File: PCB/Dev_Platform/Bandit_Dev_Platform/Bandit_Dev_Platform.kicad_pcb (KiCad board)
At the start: 4 copper layers, 50 x 30 mm, 108 parts, among them J1 Conn_01x03_Pin, J10 Conn_01x05_Pin, J11 Conn_01x05_Pin, J3 Conn_01x05_Pin, J4 Conn_01x05_Pin, J8 Conn_01x05_Pin, J9 Conn_01x06_Pin, P1 USB_C_Plug_USB2.0, SW1 SW_SPST, U1 AD7253, U2 RP2040, U3 AP2210N-4.0TRG1, U4 NCP164ASNADJT1G, U5 W25Q32JVSS, U6 MCP6486UT-E/OT, U7 MCP6S92-E/SN, U8 OPA1664, U9 OPA1664, Y1 12MHz

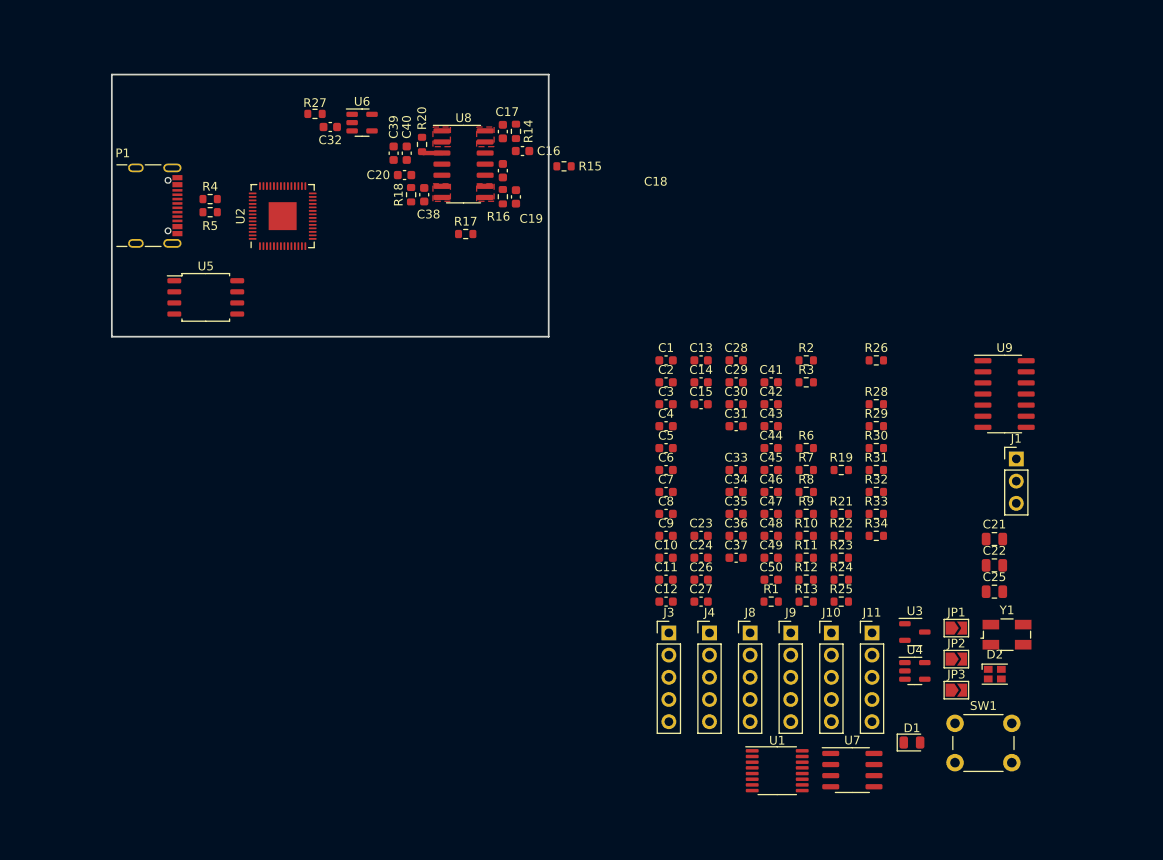
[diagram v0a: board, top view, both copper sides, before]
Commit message: update pcb, filter kinda done
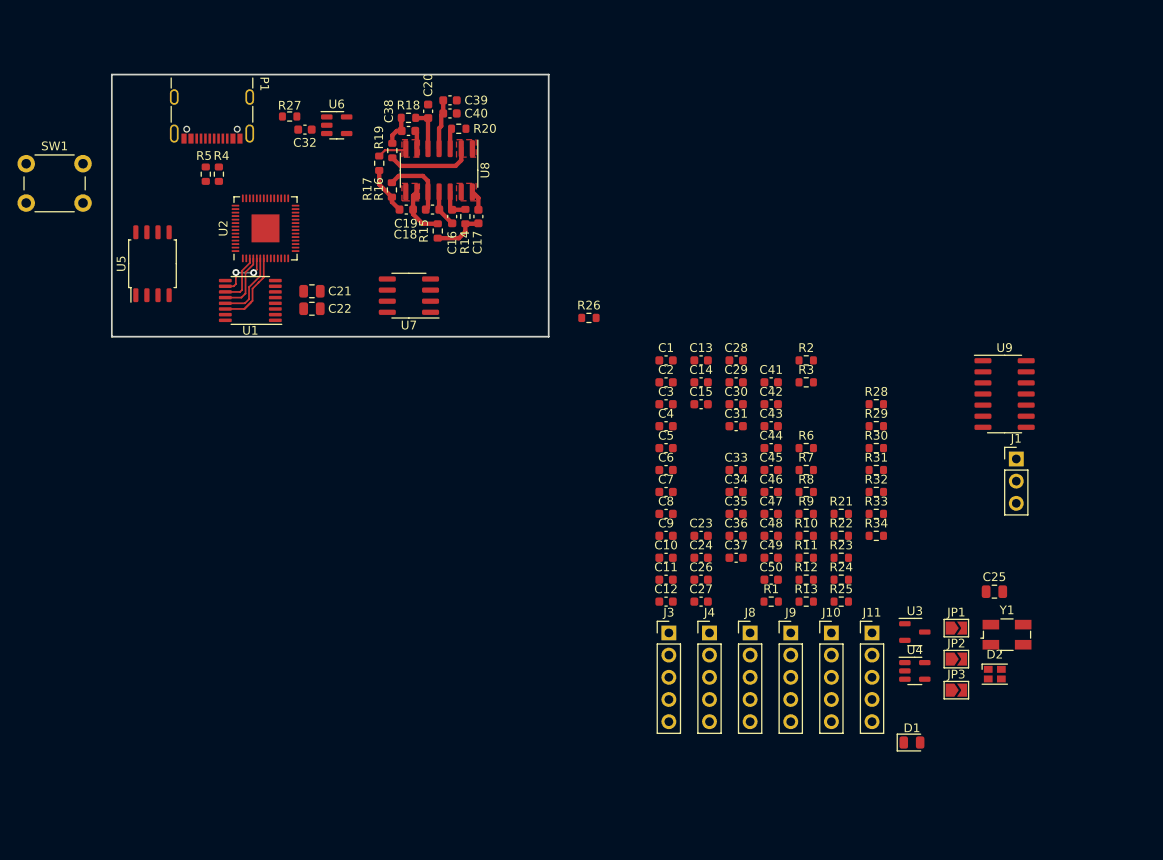
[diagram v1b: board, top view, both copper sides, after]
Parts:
- C16: value 15p C0G -> 15p C0G
- C17: value 330p C0G -> 330p C0G
- C19: value 150p C0G -> 150p C0G
- C38: value 100p C0G -> 100p C0G
- moved SW1 124.1 mm to (10.2, 30.2)
- moved C22 83.4 mm to (42.9, 46.8)
- moved C21 83.1 mm to (42.9, 44.8)
- moved U1 80.8 mm to (35.9, 45.9), turned to 180 degrees
- moved U7 74.3 mm to (54.0, 45.3), turned to 180 degrees
- moved R19 63.1 mm to (52.1, 28.7), turned to 90 degrees
- moved R26 33.2 mm to (74.6, 47.9)
- moved R15 16.2 mm to (57.3, 37.9), turned to -90 degrees
- moved P1 13.7 mm to (31.5, 23.6), turned to 180 degrees
- moved R17 12.8 mm to (50.6, 30.1), turned to -90 degrees
- moved R16 12.7 mm to (52.0, 33.2)
- moved C19 12.6 mm to (53.7, 35.5), turned to 180 degrees
- moved R14 11.3 mm to (60.5, 36.2), turned to 90 degrees
- moved C16 11.0 mm to (59.0, 36.2), turned to 90 degrees
- moved C17 10.1 mm to (62.0, 36.2), turned to -90 degrees
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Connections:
- C25 pad 2: Net-(U7-CH1) -> Net-(U7-CH0)
- R25 pad 2: Net-(U7-CH1) -> Net-(U7-CH0)
- R26 pad 1: Net-(U7-CH1) -> Net-(U7-CH0)
- U7 pad 2: /WGN_OUT -> Net-(U7-CH0)
- U7 pad 3: Net-(U7-CH1) -> /WGN_OUT
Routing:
- net Net-(U8A--): track 0.00 -> 10.7 mm
- net /ADC_SDO_B: track 0.00 -> 9.92 mm
- net /ADC_SDO_A: track 0.00 -> 8.11 mm
- net Net-(U8C-+): track 0.00 -> 8.07 mm
- net /ADC_SCK: track 0.00 -> 6.89 mm
- net /ADC_SDI: track 0.00 -> 6.47 mm, vias 0 -> 2
- net Net-(U8C--): track 0.00 -> 6.01 mm
- net /ADC_CSN: track 0.00 -> 5.99 mm
- net Net-(C17-Pad2): track 0.00 -> 5.89 mm
- net VDDA: track 0.00 -> 5.72 mm
- net Net-(U8B--): track 0.00 -> 5.49 mm
- net Net-(C19-Pad2): track 0.00 -> 5.44 mm
- net Net-(U8B-+): track 0.00 -> 4.94 mm
- net GNDA: track 0.00 -> 4.22 mm
- net Net-(C38-Pad2): track 0.00 -> 3.73 mm
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
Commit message: Josh said the tracks are great
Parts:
- removed C10, C7: 15p COG, Capacitor_SMD:C_0603_1608Metric
- removed Y1: 12MHz, Crystal:Crystal_SMD_EuroQuartz_MJ-4Pin_5.0x3.2mm
- added C17: 100n, Capacitor_SMD:C_0603_1608Metric, F.Cu at (52.4, 70.2)
- added C18: 10n, Capacitor_SMD:C_0603_1608Metric, F.Cu at (52.4, 72.7)
- added C51: 15p C0G, Capacitor_SMD:C_0603_1608Metric, F.Cu at (52.5, 45.1)
- added C52: 330p C0G, Capacitor_SMD:C_0603_1608Metric, F.Cu at (52.5, 48.1)
- added C53: 47p C0G, Capacitor_SMD:C_0603_1608Metric, F.Cu at (53.4, 42.9)
- added C54: 150p C0G, Capacitor_SMD:C_0603_1608Metric, F.Cu at (53.4, 39.9)
- added C55: 68p C0G, Capacitor_SMD:C_0603_1608Metric, F.Cu at (64.6, 42.4)
- added C56: 100p C0G, Capacitor_SMD:C_0603_1608Metric, F.Cu at (62.4, 40.1)
- added C57: 100n, Capacitor_SMD:C_0603_1608Metric, F.Cu at (65.8, 44.9)
- added C58: 10n, Capacitor_SMD:C_0603_1608Metric, F.Cu at (64.3, 44.9)
- added J5: BNC, ADS8584SIPM:BNC_THT, F.Cu at (75.9, 44.4)
- added J6: BNC, ADS8584SIPM:BNC_THT, F.Cu at (75.9, 27.6)
- added R35: 15k1, Resistor_SMD:R_0603_1608Metric, F.Cu at (52.5, 46.6)
- added R36: 8k4, Resistor_SMD:R_0603_1608Metric, F.Cu at (50.9, 43.5)
- added R37: 15k2, Resistor_SMD:R_0603_1608Metric, F.Cu at (55.6, 38.2)
- added R38: 5k9, Resistor_SMD:R_0603_1608Metric, F.Cu at (58.6, 36.8)
- added R39: 14k8, Resistor_SMD:R_0603_1608Metric, F.Cu at (63.9, 40.1)
- added R40: 6k3, Resistor_SMD:R_0603_1608Metric, F.Cu at (60.1, 38.3)
- added R41: 11k7, Resistor_SMD:R_0603_1608Metric, F.Cu at (62.6, 45.9)
- added U10: OPA1664, Package_SO:SOIC-14_3.9x8.7mm_P1.27mm, F.Cu at (57.9, 43.6)
- added X1: SG-210STF, Oscillator:Oscillator_SMD_SeikoEpson_SG210-4Pin_2.5x2.0mm, F.Cu at (41.1, 28.9)
- moved C25 71.6 mm to (68.5, 30.5), turned to 90 degrees
- moved R22 67.7 mm to (44.2, 40.0), turned to 180 degrees
- moved R24 66.8 mm to (44.2, 47.1), turned to 180 degrees
- moved R21 65.9 mm to (44.2, 41.5), turned to 180 degrees
- moved R23 65.0 mm to (44.2, 48.6), turned to 180 degrees
- moved R25 64.5 mm to (66.5, 27.5), turned to -90 degrees
- moved C23 55.7 mm to (41.9, 40.8), turned to -90 degrees
- moved C24 53.2 mm to (41.9, 47.9), turned to 90 degrees
- moved R26 22.5 mm to (65.0, 27.5), turned to 90 degrees
- moved U7 16.0 mm to (64.3, 33.0), turned to -90 degrees
- moved C52 15.0 mm to (47.0, 35.5), turned to 180 degrees
- moved P1 14.5 mm to (23.7, 35.9), turned to -90 degrees
- moved R36 13.9 mm to (45.3, 30.9), turned to 180 degrees
- moved R35 13.7 mm to (47.0, 34.0), turned to 0 degrees
- moved C51 12.6 mm to (47.0, 32.5), turned to 0 degrees
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- renumbered C16 to C51, C17 to C52, C18 to C53, C19 to C54, C20 to C55, C38 to C56, C39 to C57, C40 to C58, R14 to R35, R15 to R36, R16 to R37, R17 to R38, R18 to R39, R19 to R40, R20 to R41, U8 to U10
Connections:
- R22 pad 1: /SE_SIG_B -> /SE_SIG_A
- R23 pad 1: /SE_SIG_A -> /SE_SIG_B
- U2 pad 20: /XIN -> /CLK_12M
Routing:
- net /WGN_OUT: track 0.00 -> 60.2 mm
- net /SIG_IN: track 0.00 -> 21.4 mm
- net Net-(J2-In): track 0.00 -> 16.0 mm
- net /SE_SIG_B: track 0.00 -> 11.2 mm
- net Net-(U10A--): track 10.7 -> 21.3 mm
- net Net-(U10C-+): track 8.07 -> 16.1 mm
- net Net-(U7-CH0): track 0.00 -> 6.31 mm
- net Net-(U10C--): track 6.01 -> 12.0 mm
- net /SE_SIG_A: track 2.34 -> 8.23 mm
- net Net-(C52-Pad2): track 5.89 -> 11.8 mm
- net VDDA: track 5.72 -> 11.4 mm
- net Net-(U1-AINP_B): track 0.00 -> 5.54 mm
- net Net-(U1-AINP_A): track 0.00 -> 5.50 mm
- net Net-(U10B--): track 5.49 -> 11.0 mm
- net Net-(C54-Pad2): track 5.44 -> 10.9 mm
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- added copper zone on F.Cu, net /SE_SIG_B
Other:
- board size 50 x 30 mm -> 63.5 x 31.8 mm

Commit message: Fixing dev pcb
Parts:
- removed the C51 at (52.5, 45.1)
- removed the C51 at (47.0, 32.5)
- removed the C52 at (47.0, 35.5)
- removed the C52 at (52.5, 48.1)
- removed the C53 at (47.8, 30.2)
- removed the C53 at (53.4, 42.9)
- removed the C54 at (47.8, 27.2)
- removed the C54 at (53.4, 39.9)
- removed the C55 at (59.0, 29.8)
- removed the C55 at (64.6, 42.4)
- removed the C56 at (62.4, 40.1)
- removed the C56 at (56.8, 27.5)
- removed the C57 at (60.2, 32.2)
- removed the C57 at (65.8, 44.9)
- removed the C58 at (58.8, 32.2)
- removed the C58 at (64.3, 44.9)
- removed the R35 at (47.0, 34.0)
- removed the R35 at (52.5, 46.6)
- removed the R36 at (45.3, 30.9)
- removed the R36 at (50.9, 43.5)
- removed the R37 at (50.0, 25.6)
- removed the R37 at (55.6, 38.2)
- removed the R38 at (53.0, 24.1)
- removed the R38 at (58.6, 36.8)
- removed the R39 at (58.2, 27.5)
- removed the R39 at (63.9, 40.1)
- removed the R40 at (54.5, 25.6)
- removed the R40 at (60.1, 38.3)
- removed the R41 at (62.6, 45.9)
- removed the R41 at (57.0, 33.2)
- removed the U10 at (57.9, 43.6)
- removed the U10 at (52.2, 31.0)
- added C10: 15p COG, Capacitor_SMD:C_0603_1608Metric, F.Cu at (91.5, 80.9)
- added C51: 15p C0G, Capacitor_SMD:C_0603_1608Metric, F.Cu at (103.5, 70.9)
- added C52: 330p C0G, Capacitor_SMD:C_0603_1608Metric, F.Cu at (103.5, 73.4)
- added C53: 47p C0G, Capacitor_SMD:C_0603_1608Metric, F.Cu at (103.5, 75.9)
- added C54: 150p C0G, Capacitor_SMD:C_0603_1608Metric, F.Cu at (103.5, 78.4)
- added C55: 68p C0G, Capacitor_SMD:C_0603_1608Metric, F.Cu at (103.5, 80.9)
- added C56: 100p C0G, Capacitor_SMD:C_0603_1608Metric, F.Cu at (103.5, 83.5)
- added C57: 100n, Capacitor_SMD:C_0603_1608Metric, F.Cu at (103.5, 86.0)
- added C58: 10n, Capacitor_SMD:C_0603_1608Metric, F.Cu at (107.5, 58.4)
- added C7: 15p COG, Capacitor_SMD:C_0603_1608Metric, F.Cu at (91.5, 73.4)
- added R35: 15k1, Resistor_SMD:R_0603_1608Metric, F.Cu at (115.5, 68.4)
- added R36: 8k4, Resistor_SMD:R_0603_1608Metric, F.Cu at (115.5, 70.9)
- added R37: 15k2, Resistor_SMD:R_0603_1608Metric, F.Cu at (115.5, 73.4)
- added R38: 5k9, Resistor_SMD:R_0603_1608Metric, F.Cu at (115.5, 75.9)
- added R39: 14k8, Resistor_SMD:R_0603_1608Metric, F.Cu at (115.5, 78.4)
- added R40: 6k3, Resistor_SMD:R_0603_1608Metric, F.Cu at (115.5, 80.9)
- added R41: 11k7, Resistor_SMD:R_0603_1608Metric, F.Cu at (115.5, 83.5)
- added U10: OPA1664, Package_SO:SOIC-14_3.9x8.7mm_P1.27mm, F.Cu at (63.3, 32.0)
- added Y1: 12MHz, Crystal:Crystal_SMD_EuroQuartz_MJ-4Pin_5.0x3.2mm, F.Cu at (110.3, 104.5)
- moved SW1 133.8 mm to (129.1, 91.7)
- moved U6 113.1 mm to (120.1, 100.8), turned to 0 degrees
- moved X1 110.9 mm to (136.7, 85.3), turned to 0 degrees
- moved C22 94.1 mm to (135.6, 61.6)
- moved C21 94.0 mm to (135.6, 58.6)
- moved R27 91.0 mm to (111.5, 78.4), turned to 0 degrees
- moved U7 81.6 mm to (102.4, 105.2), turned to 0 degrees
- moved C25 75.3 mm to (135.6, 64.6), turned to 0 degrees
- moved C32 73.0 mm to (99.5, 60.9), turned to 0 degrees
- moved R22 72.1 mm to (111.5, 65.9), turned to 0 degrees
- moved R24 71.4 mm to (111.5, 70.9), turned to 0 degrees
- moved R21 70.8 mm to (111.5, 63.4), turned to 0 degrees
- moved R23 70.2 mm to (111.5, 68.4), turned to 0 degrees
- moved R26 67.1 mm to (111.5, 75.9), turned to 0 degrees
- moved J6 66.1 mm to (123.1, 73.9)
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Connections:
- C44 pad 2: Net-(U9C-+) -> Net-(U9A-+)
- C45 pad 1: Net-(U9C--) -> Net-(U9A--)
- C50 pad 2: Net-(U9A-+) -> Net-(U9C-+)
- R29 pad 1: Net-(U9C--) -> Net-(U9A--)
- R30 pad 2: Net-(U9C-+) -> Net-(U9A-+)
- R33 pad 1: Net-(U9A--) -> Net-(U9C--)
- R34 pad 2: Net-(U9A-+) -> Net-(U9C-+)
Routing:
- net /WGN_OUT: track 60.2 -> 0.00 mm
- net /FLASH_IO3: track 0.00 -> 22.5 mm
- net /SIG_IN: track 21.4 -> 0.00 mm
- net Net-(U10A--): track 21.3 -> 0.00 mm
- net /FLASH_SCK: track 0.00 -> 19.9 mm
- net /FLASH_IO0: track 0.00 -> 17.1 mm
- net Net-(U10C-+): track 16.1 -> 0.00 mm
- net Net-(J2-In): track 16.0 -> 0.00 mm
- net /~{FLASH_CSN}: track 0.00 -> 13.8 mm
- net /FLASH_IO1: track 0.00 -> 12.5 mm
- net Net-(U10C--): track 12.0 -> 0.00 mm
- net Net-(C52-Pad2): track 11.8 -> 0.00 mm
- net /FLASH_IO2: track 0.00 -> 11.5 mm
- net VDDA: track 11.4 -> 0.00 mm
- net /SE_SIG_B: track 11.2 -> 0.00 mm
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- removed copper zone on F.Cu, net /SE_SIG_A
- removed copper zone on F.Cu, net /SE_SIG_B
- removed copper zone on F.Cu, net Net-(U10A--)
- removed copper zone on F.Cu, net Net-(U10B--)
- removed copper zone on F.Cu, net Net-(U10C--)
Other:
- board text added: "A6: D+ A7: D- B6: D+ B7: D-"

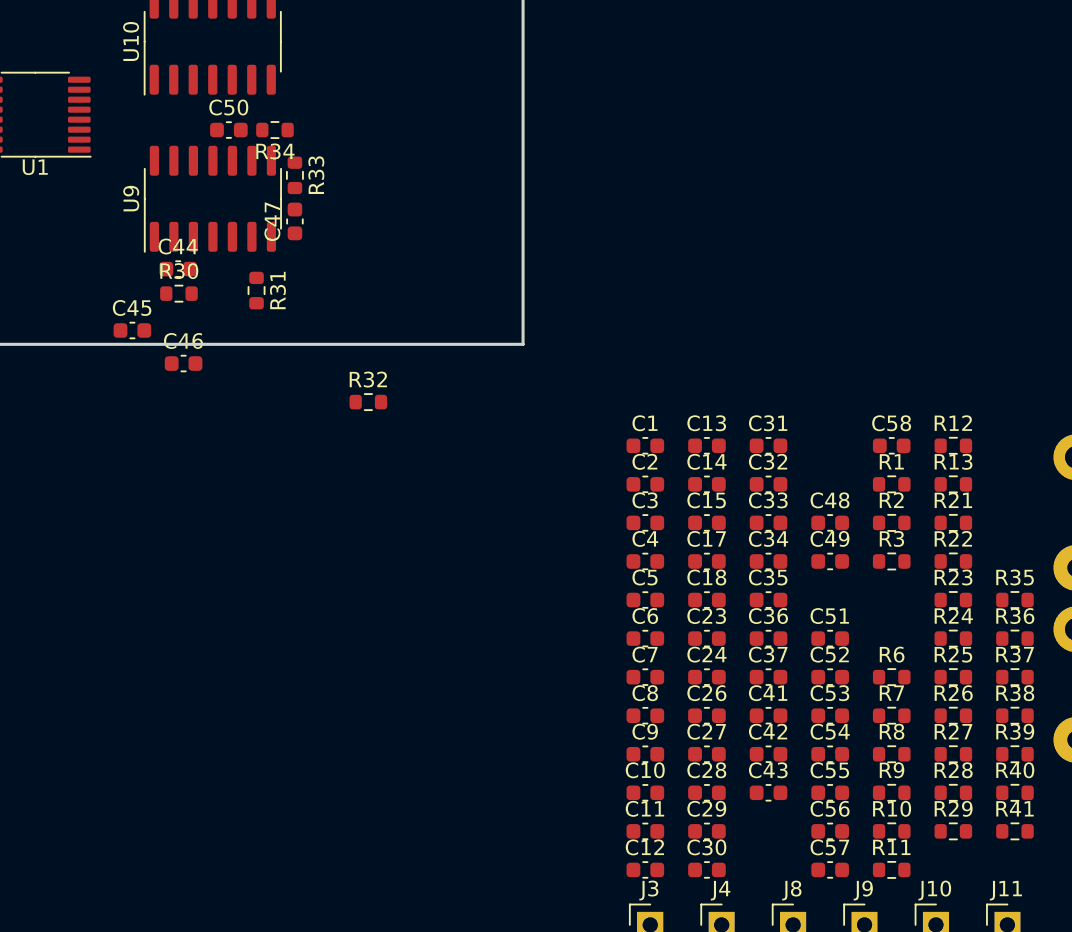
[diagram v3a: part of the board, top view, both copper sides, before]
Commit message: Initial USB protocol draft
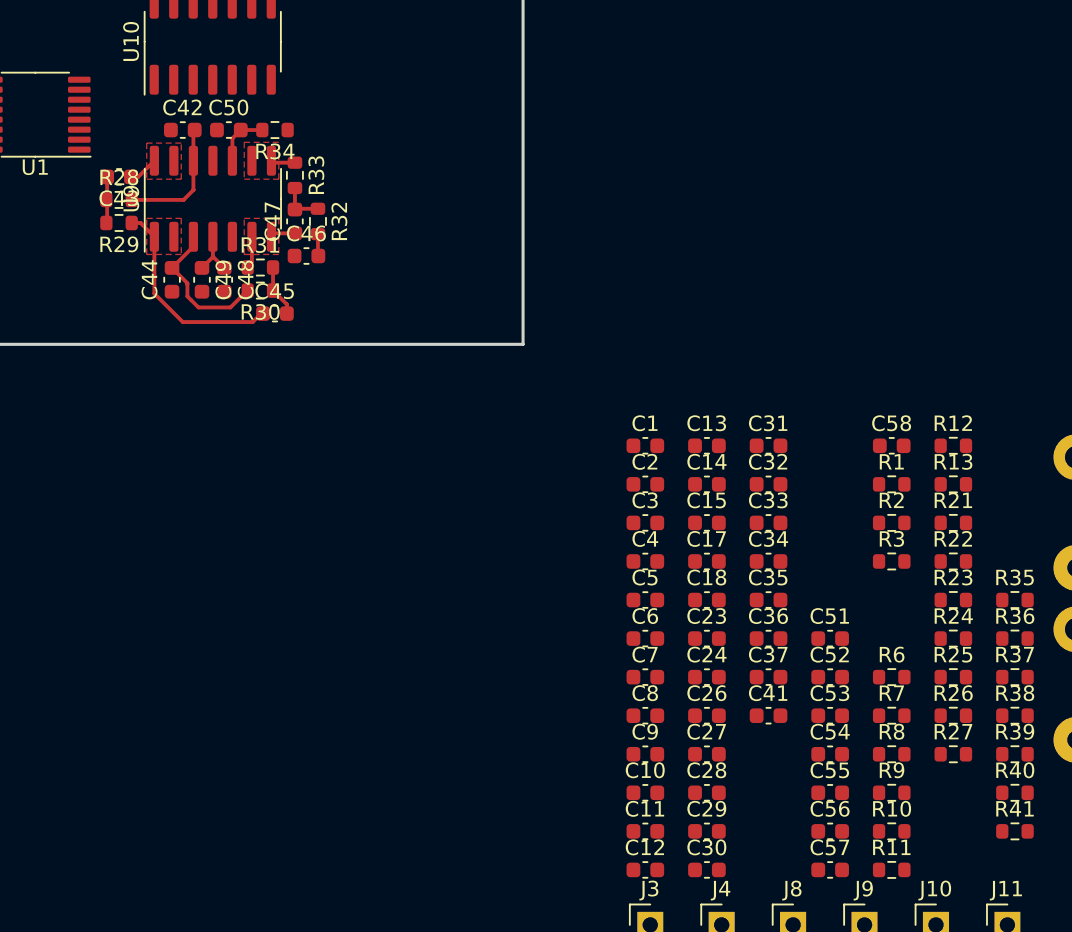
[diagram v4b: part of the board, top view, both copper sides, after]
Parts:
- moved R29 67.2 mm to (57.2, 43.9), turned to 180 degrees
- moved R28 66.6 mm to (57.2, 42.4)
- moved C43 58.3 mm to (57.2, 40.9), turned to 180 degrees
- moved C42 55.7 mm to (61.4, 37.8)
- moved C49 44.8 mm to (62.6, 47.5), turned to -90 degrees
- moved C48 42.5 mm to (64.0, 47.5), turned to -90 degrees
- moved R32 12.2 mm to (70.2, 43.8), turned to -90 degrees
- moved C46 10.6 mm to (69.4, 46.0)
- moved C45 9.34 mm to (67.3, 49.8)
- moved R30 5.30 mm to (66.4, 48.2), turned to 180 degrees
- moved R31 1.52 mm to (66.4, 46.8), turned to 0 degrees
- moved C44 0.81 mm to (60.6, 47.5), turned to 90 degrees
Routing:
- net Net-(U9A--): track 0.00 -> 13.6 mm
- net Net-(U9A-+): track 0.00 -> 9.55 mm
- net Net-(U9D-+): track 0.00 -> 8.23 mm
- net Net-(U9B--): track 0.00 -> 3.74 mm
- net Net-(U9C-+): track 0.00 -> 3.63 mm
- net Net-(C45-Pad2): track 0.00 -> 3.52 mm
- net VDDA: track 0.00 -> 3.37 mm
- net Net-(C43-Pad2): track 0.00 -> 3.02 mm
- net Net-(C47-Pad2): track 0.00 -> 2.92 mm
- net /SE_SIG_B: track 0.00 -> 1.96 mm
- net Net-(U9C--): track 0.00 -> 1.58 mm
- net Net-(U9B-+): track 0.00 -> 1.44 mm
- added copper zone on F.Cu, net /SE_SIG_B
- added copper zone on In1.Cu, net GND
- added copper zone on In1.Cu, net GNDA
- added copper zone on F.Cu, net Net-(U9A--)
- added copper zone on F.Cu, net Net-(U9B--)
- added copper zone on F.Cu, net Net-(U9C--)

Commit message: PCB Fun
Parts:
- moved C57 73.5 mm to (63.9, 24.1), turned to 90 degrees
- moved R36 72.4 mm to (57.0, 28.2), turned to 180 degrees
- moved R38 70.9 mm to (66.5, 24.7)
- moved C54 70.2 mm to (59.1, 24.0), turned to 90 degrees
- moved R37 70.1 mm to (66.5, 23.2), turned to 180 degrees
- moved R35 70.1 mm to (57.0, 29.8)
- moved R41 69.2 mm to (67.4, 33.7), turned to 180 degrees
- moved R40 68.3 mm to (68.5, 31.4), turned to 90 degrees
- moved R39 67.6 mm to (69.2, 29.2), turned to 180 degrees
- moved C53 67.4 mm to (60.5, 24.0), turned to -90 degrees
- moved C56 66.7 mm to (69.3, 26.2)
- moved C55 63.3 mm to (69.2, 27.7), turned to 180 degrees
- moved C52 62.7 mm to (57.0, 31.3), turned to 180 degrees
- moved C58 56.7 mm to (62.4, 24.1), turned to 90 degrees
- moved C51 56.4 mm to (61.1, 33.7)
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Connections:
- C41 pad 2: Net-(U10B-+) -> Net-(U10D-+)
- C51 pad 2: Net-(U10A-+) -> Net-(U10C-+)
- C53 pad 2: Net-(U10D-+) -> Net-(U10B-+)
- C54 pad 1: Net-(U10D--) -> Net-(U10B--)
- C55 pad 2: Net-(U10C-+) -> Net-(U10A-+)
- C56 pad 1: Net-(U10C--) -> Net-(U10A--)
- R35 pad 2: Net-(U10A-+) -> Net-(U10C-+)
- R36 pad 1: Net-(U10D--) -> Net-(U10B--)
- R37 pad 2: Net-(U10D-+) -> Net-(U10B-+)
- R38 pad 1: Net-(U10C--) -> Net-(U10A--)
- R39 pad 2: Net-(U10C-+) -> Net-(U10A-+)
- R40 pad 1: Net-(U10B--) -> Net-(U10D--)
- R41 pad 2: Net-(U10B-+) -> Net-(U10D-+)
- U10 pad 1: /SE_SIG_A -> Net-(U10A--)
- U10 pad 2: /SE_SIG_A -> Net-(U10A--)
- U10 pad 8: Net-(U10C--) -> /SE_SIG_A
- U10 pad 9: Net-(U10C--) -> /SE_SIG_A
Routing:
- net Net-(U9A--): track 13.6 -> 4.07 mm
- net Net-(C45-Pad2): track 3.52 -> 12.2 mm
- net Net-(U9B-+): track 1.44 -> 6.99 mm
- net Net-(C47-Pad2): track 2.92 -> 6.25 mm
- net Net-(U10B-+): track 0.00 -> 0.61 mm

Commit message: PCB Update
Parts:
- moved J6 63.6 mm to (77.3, 29.8)
- moved J5 49.2 mm to (77.2, 45.0)
- moved C41 0.64 mm to (63.8, 33.7)
- moved R41 0.64 mm to (66.8, 33.7)
- moved C55 0.58 mm to (69.2, 27.2)
- moved R39 0.58 mm to (69.2, 28.6)
- moved C56 0.58 mm to (69.3, 25.6)
- moved R40 0.53 mm to (68.5, 30.9)
- moved R37 0.28 mm to (66.2, 23.3)
- moved C51 0.28 mm to (60.8, 33.7)
- moved R38 0.28 mm to (66.2, 24.7)
- moved C53 0.23 mm to (60.3, 24.1)
- moved C54 0.23 mm to (58.8, 24.1)
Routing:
- net Net-(C54-Pad2): track 0.29 -> 12.9 mm
- net Net-(U10B-+): track 0.61 -> 11.3 mm
- net Net-(U10C-+): track 0.00 -> 7.43 mm
- net Net-(U10A-+): track 0.00 -> 6.81 mm
- net Net-(C56-Pad2): track 0.23 -> 6.73 mm
- net Net-(U10B--): track 0.00 -> 4.22 mm
- net Net-(U10A--): track 0.02 -> 4.15 mm
- net Net-(U10D-+): track 0.00 -> 3.41 mm
- net VDDA: track 3.37 -> 6.64 mm
- net Net-(C52-Pad2): track 0.00 -> 3.07 mm
- net /SE_SIG_A: track 0.00 -> 1.69 mm
- net Net-(U10D--): track 0.00 -> 0.96 mm
- net Net-(C47-Pad2): track 6.25 -> 6.91 mm
- added copper zone on F.Cu, net /SE_SIG_A
- added copper zone on F.Cu, net Net-(U10A--)
- added copper zone on F.Cu, net Net-(U10B--)
- added copper zone on F.Cu, net Net-(U10D--)
